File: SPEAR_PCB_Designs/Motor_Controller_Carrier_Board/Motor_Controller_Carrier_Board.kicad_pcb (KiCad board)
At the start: 2 copper layers, 7 parts, among them J1 Conn_01x02_Pin, J2 Conn_01x02_Pin, J3 Conn_01x02_Pin

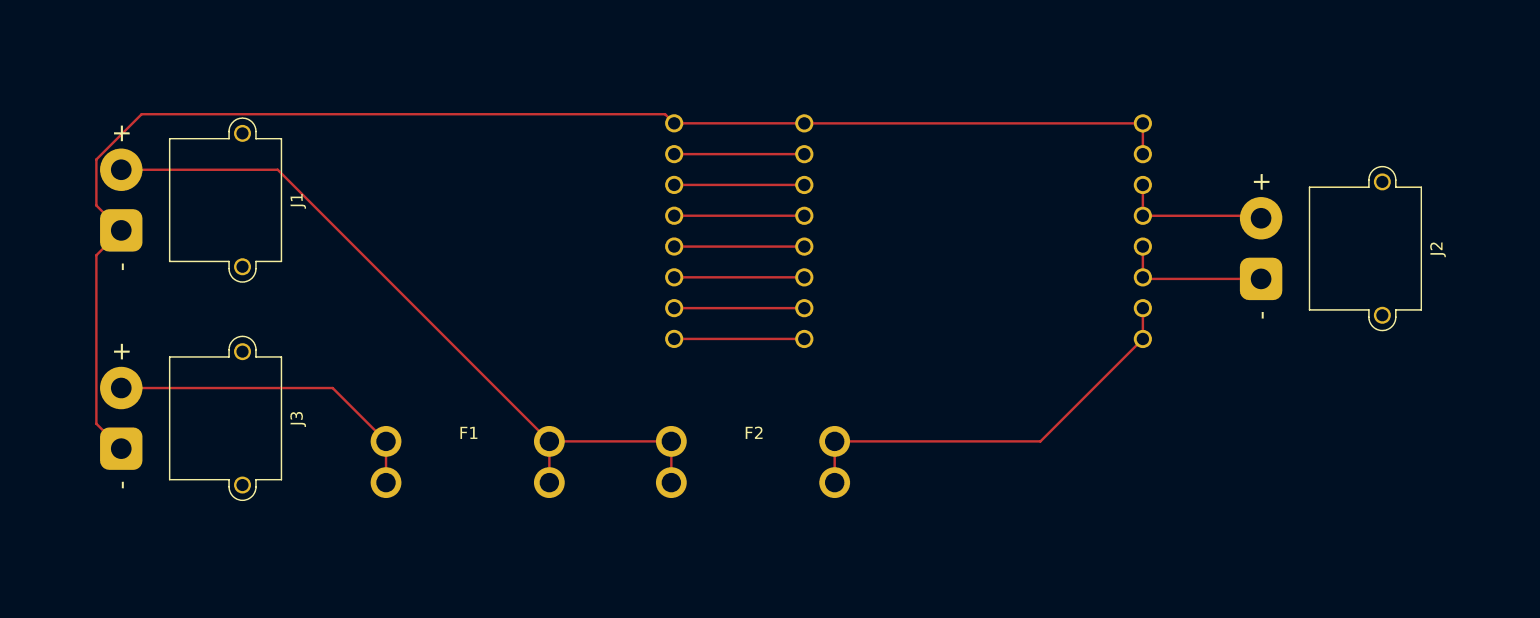
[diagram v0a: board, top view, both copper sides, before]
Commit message: added Carrier Board PCB
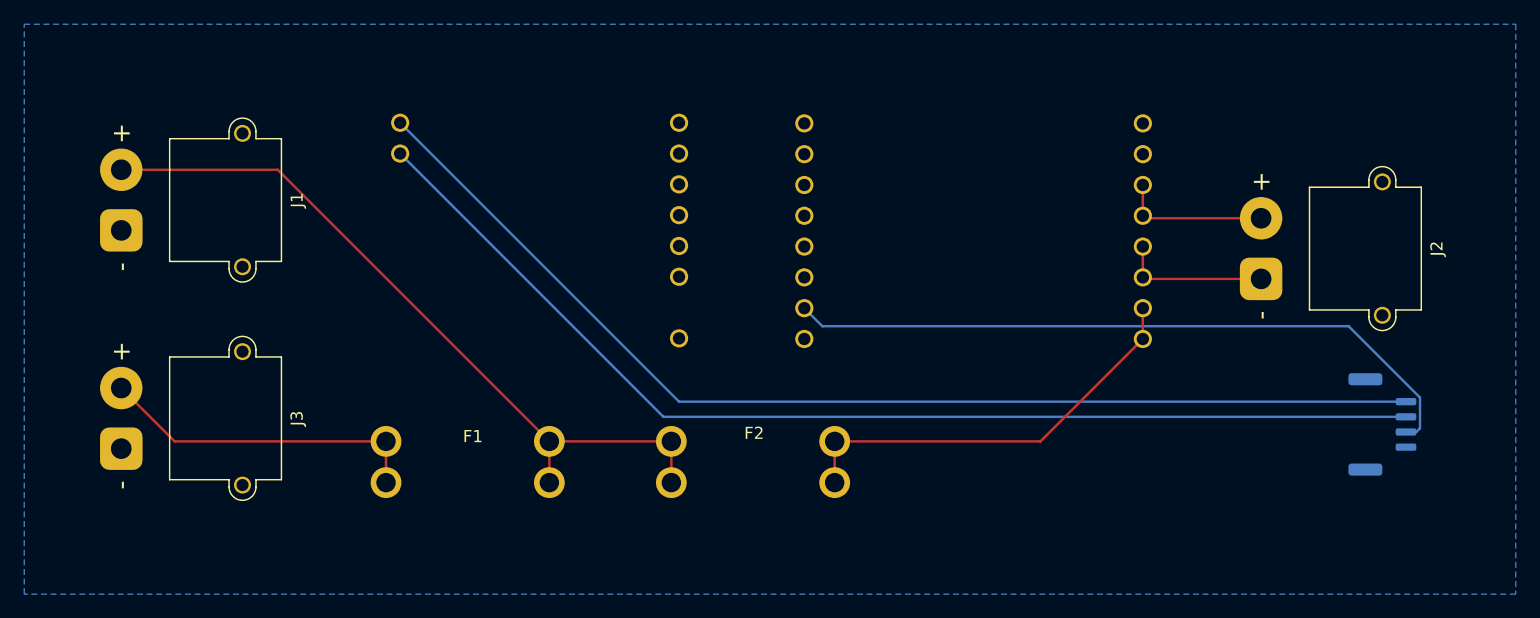
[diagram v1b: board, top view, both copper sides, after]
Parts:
- added J4: Conn_01x04_Pin, Motor_Controller_Carrier_Board:JST_GH_BM04B-GHS-TBT_1x04-1MP_P1.25mm_Vertical, B.Cu at (176.0, 103.0)
- moved MiCB1 0.40 mm to (90.0, 76.9)
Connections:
- net Net-(J1-Pin_1) renamed GND
- MDB1 pad 7: Net-(MDB1-3V3) -> Net-(J4-Pin_3)
- MiCB1 pad 7: Net-(MDB1-3V3) -> Net-(MDB1-VM)
- MiCB1 pad 8: Net-(MDB1-VM) -> Net-(J4-Pin_1)
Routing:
- net GND: track 117.1 -> 0.00 mm
- net Net-(J4-Pin_1): track 0.00 -> 92.5 mm
- net Net-(J4-Pin_2): track 0.00 -> 91.9 mm
- net Net-(J4-Pin_3): track 0.00 -> 57.6 mm
- net Net-(MDB1-DIR): track 10.7 -> 0.00 mm
- net Net-(MDB1-3V3): track 10.7 -> 0.00 mm
- net Net-(MDB1-VM): track 10.7 -> 0.00 mm
- net Net-(MDB1-SLP): track 10.7 -> 0.00 mm
- net Net-(MDB1-PWM): track 10.7 -> 0.00 mm
- net Net-(MDB1-FLT): track 10.7 -> 0.00 mm
- net Net-(MDB1-CS): track 10.7 -> 0.00 mm
- net Net-(J2-Pin_2): track 12.4 -> 13.7 mm
- added copper zone on B.Cu, net GND

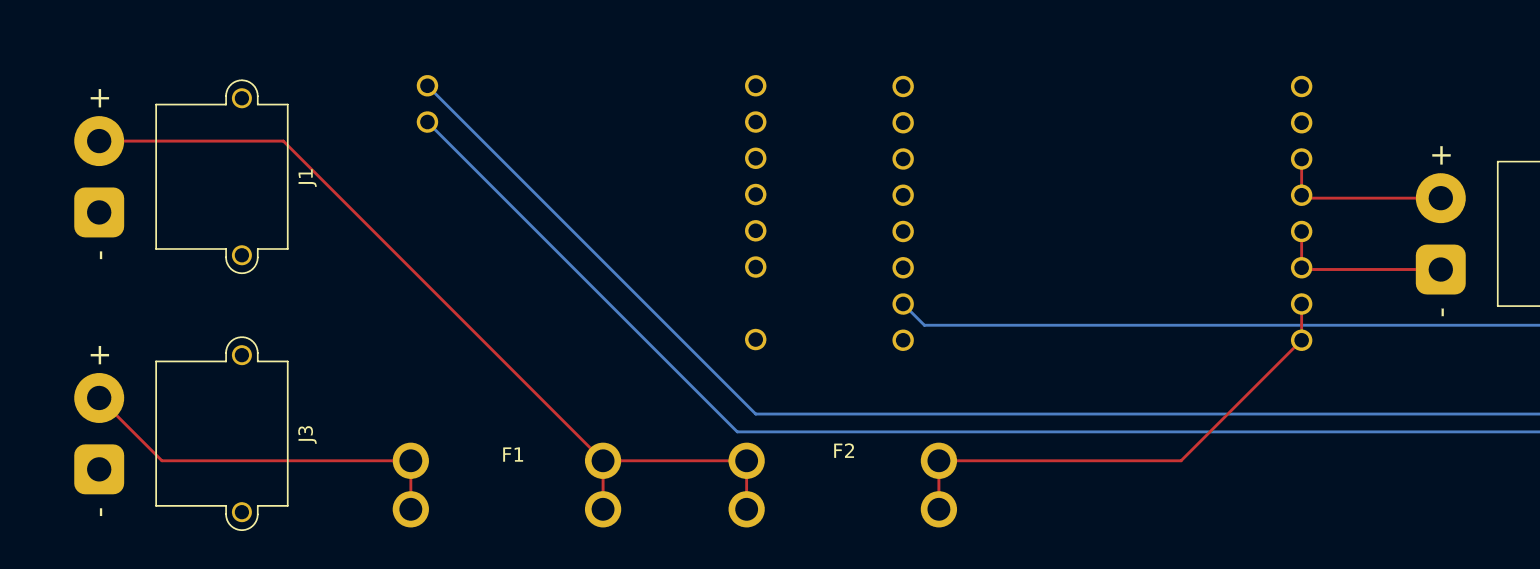
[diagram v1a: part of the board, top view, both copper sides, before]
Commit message: moved board footprints and created new motor driver board footprints
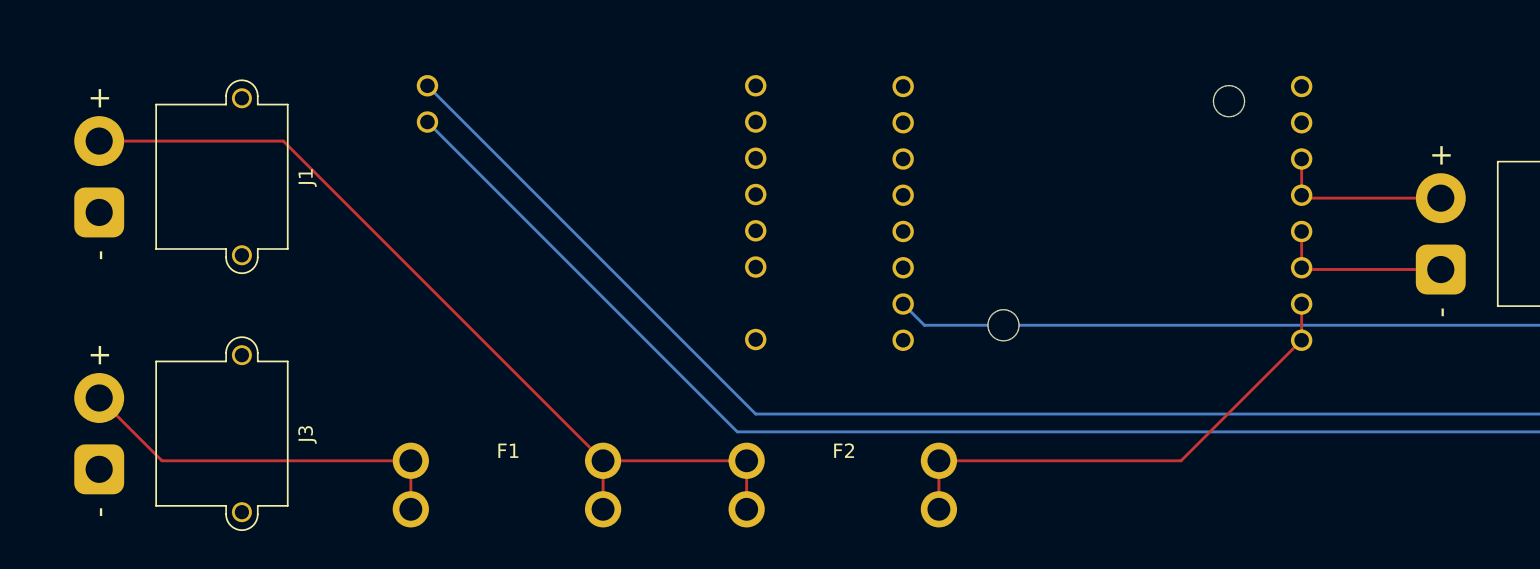
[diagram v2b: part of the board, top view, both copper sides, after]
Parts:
- J1, J2, J3: footprint XT30:AMASS_XT30PW-M -> Connector_AMASS:AMASS_XT30PW-M_1x02_P2.50mm_Horizontal
- MDB1: footprint Motor_Controller_Carrier_Board:Motor_Driver_Board -> SPEAR_Boards:Motor_Driver_Board_2992
- MiCB1: footprint Motor_Controller_Carrier_Board:Micro_Controller_Board -> SPEAR_Boards:Micro_Controller_Board

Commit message: Finished schematic and general PCB layout for carrier board 2992
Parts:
- removed MiCB1: Micro_Controller_Board, SPEAR_Boards:Micro_Controller_Board
- added C1: 10u, SPEAR_AP63203BuckConverter:CAP_FG20_TDK_C1, F.Cu at (106.8, 81.0)
- added C2: 22u, SPEAR_AP63203BuckConverter:CAP_FG22_TDK_C2_C4, F.Cu at (108.0, 51.5)
- added C3: 100n, Capacitor_THT:C_Disc_D5.0mm_W2.5mm_P5.00mm, F.Cu at (106.2, 73.0)
- added C4: 22u, SPEAR_AP63203BuckConverter:CAP_FG22_TDK_C2_C4, F.Cu at (102.5, 51.5)
- added C5: C, Motor_Controller_Carrier_Board:CAP_UBY_18X20_NCH, F.Cu at (162.0, 100.5)
- added L1: 3.9u, SPEAR_AP63203BuckConverter:L_Wurth_WE-LHMI-1040_L1, F.Cu at (104.0, 65.0)
- added MCB1: Micro_Controller_Board, SPEAR_Boards:Micro_Controller_Board, F.Cu at (167.7, 50.0)
- added U1: AP63203WU, Package_TO_SOT_SMD:TSOT-23-6, F.Cu at (102.0, 78.1)
- F1, F2: value Fuse -> 3557-10; footprint Motor_Controller_Carrier_Board:Fuse -> Motor_Controller_Carrier_Board:FUSE_3557-10
- J4: value Conn_01x04_Pin -> JST_S4B-XH-A-1; footprint Motor_Controller_Carrier_Board:JST_GH_BM04B-GHS-TBT_1x04-1MP_P1.25mm_Vertical -> Connector_JST:JST_XH_S4B-XH-A-1_1x04_P2.50mm_Horizontal; moved to F.Cu
- MDB1: value Motor_Driver_Board -> Motor_Driver_Board_2992
- moved J3 104.2 mm to (176.0, 111.0)
- moved J2 67.0 mm to (99.0, 89.0), turned to 90 degrees
- moved MDB1 64.0 mm to (190.1, 65.6), turned to -90 degrees
- moved J4 42.5 mm to (174.0, 60.5), turned to 90 degrees
- moved J1 32.5 mm to (98.7, 105.5), turned to 90 degrees
- moved F1 26.4 mm to (117.0, 105.0), turned to 90 degrees
- moved F2 6.60 mm to (108.0, 105.0), turned to 90 degrees
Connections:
- J2 pad 1: Net-(J2-Pin_1) -> GND
- J3 pad 1: GND -> Net-(J3-Pin_1)
- J4 pad 1: Net-(J4-Pin_1) -> /ENC_B
- J4 pad 2: Net-(J4-Pin_2) -> /ENC_A
- J4 pad 3: Net-(J4-Pin_3) -> GND
- J4 pad 4: GND -> +3.3V
- MDB1 pad 11: Net-(J2-Pin_2) -> Net-(J3-Pin_2)
- MDB1 pad 12: Net-(J2-Pin_2) -> Net-(J3-Pin_2)
- MDB1 pad 13: Net-(J2-Pin_1) -> Net-(J3-Pin_1)
- MDB1 pad 14: Net-(J2-Pin_1) -> Net-(J3-Pin_1)
- MDB1 pad 15: Net-(F2-Pad2) -> +BATT
- MDB1 pad 16: Net-(F2-Pad2) -> +BATT
- MDB1 pad 2: Net-(MDB1-DIR) -> /DIR
- MDB1 pad 3: Net-(MDB1-PWM) -> /PWM
- MDB1 pad 4: Net-(MDB1-SLP) -> /SLP
- MDB1 pad 5: Net-(MDB1-FLT) -> /FLT
- MDB1 pad 6: Net-(MDB1-CS) -> /CS
- MDB1 pad 7: Net-(J4-Pin_3) -> unconnected-(MDB1-3V3-Pad7)
- MDB1 pad 8: Net-(MDB1-VM) -> unconnected-(MDB1-VM-Pad8)
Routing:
- net +3.3V: track 0.00 -> 102.0 mm
- net Net-(J4-Pin_1): track 92.5 -> 0.00 mm
- net Net-(J4-Pin_2): track 91.9 -> 0.00 mm
- net +BATT: track 0.00 -> 85.2 mm
- net /ENC_B: track 0.00 -> 61.7 mm
- net Net-(J4-Pin_3): track 57.6 -> 0.00 mm
- net /CS: track 0.00 -> 48.5 mm
- net Net-(J1-Pin_2): track 61.4 -> 20.5 mm
- net /FLT: track 0.00 -> 35.6 mm
- net Net-(F2-Pad2): track 34.9 -> 0.00 mm
- net /SLP: track 0.00 -> 34.7 mm
- net /PWM: track 0.00 -> 34.1 mm
- net /DIR: track 0.00 -> 33.8 mm
- net /ENC_A: track 0.00 -> 28.4 mm
- net Net-(J3-Pin_1): track 0.00 -> 21.3 mm
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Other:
- board outline added: 192 x 103 mm

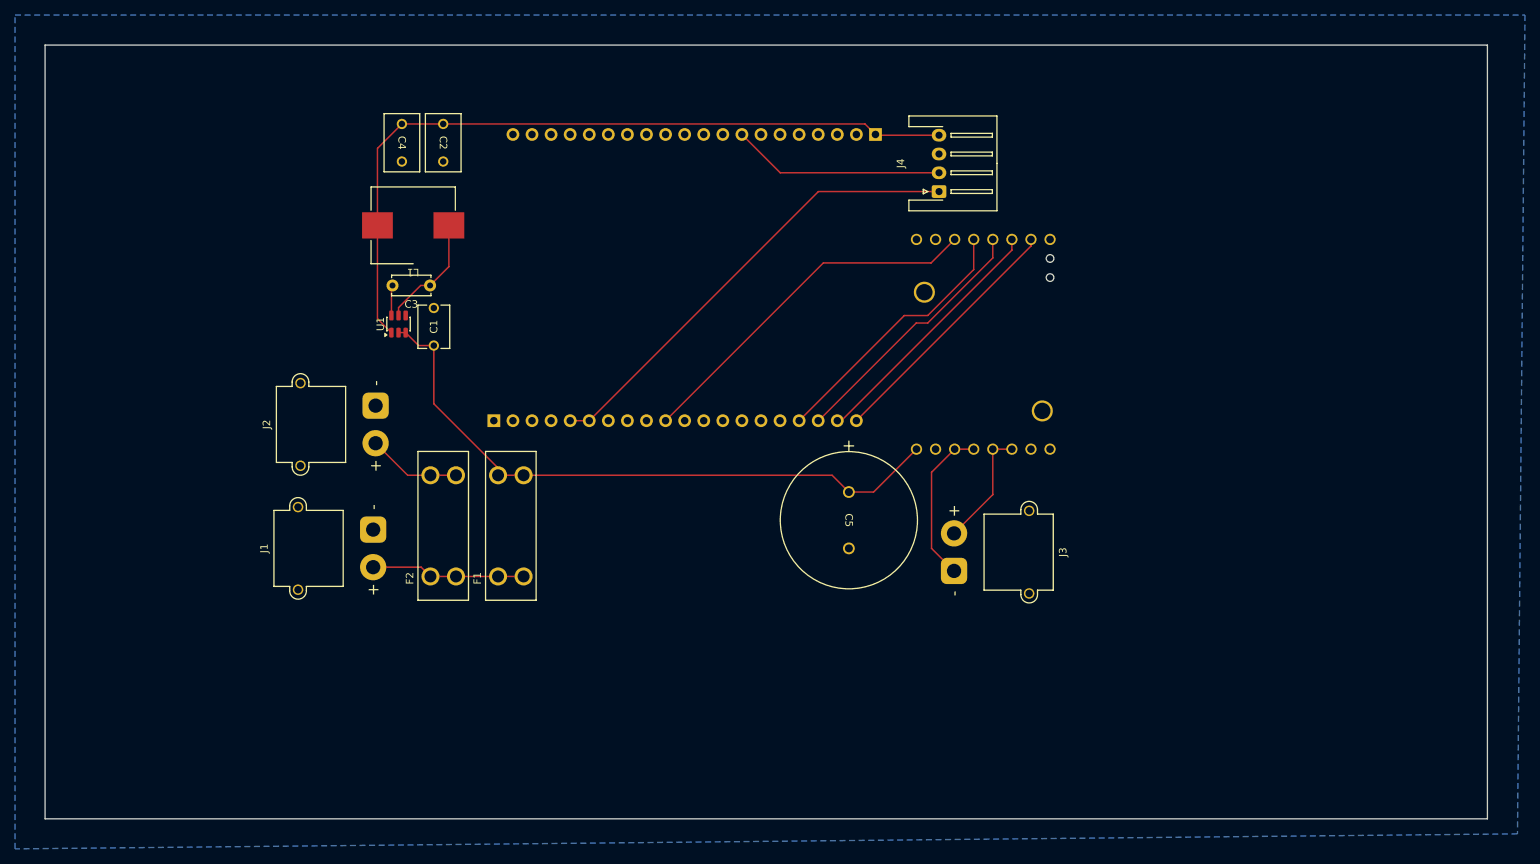
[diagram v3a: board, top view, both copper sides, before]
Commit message: Added silkscreen and courtyards to board footprints and 3D models to the carrier board
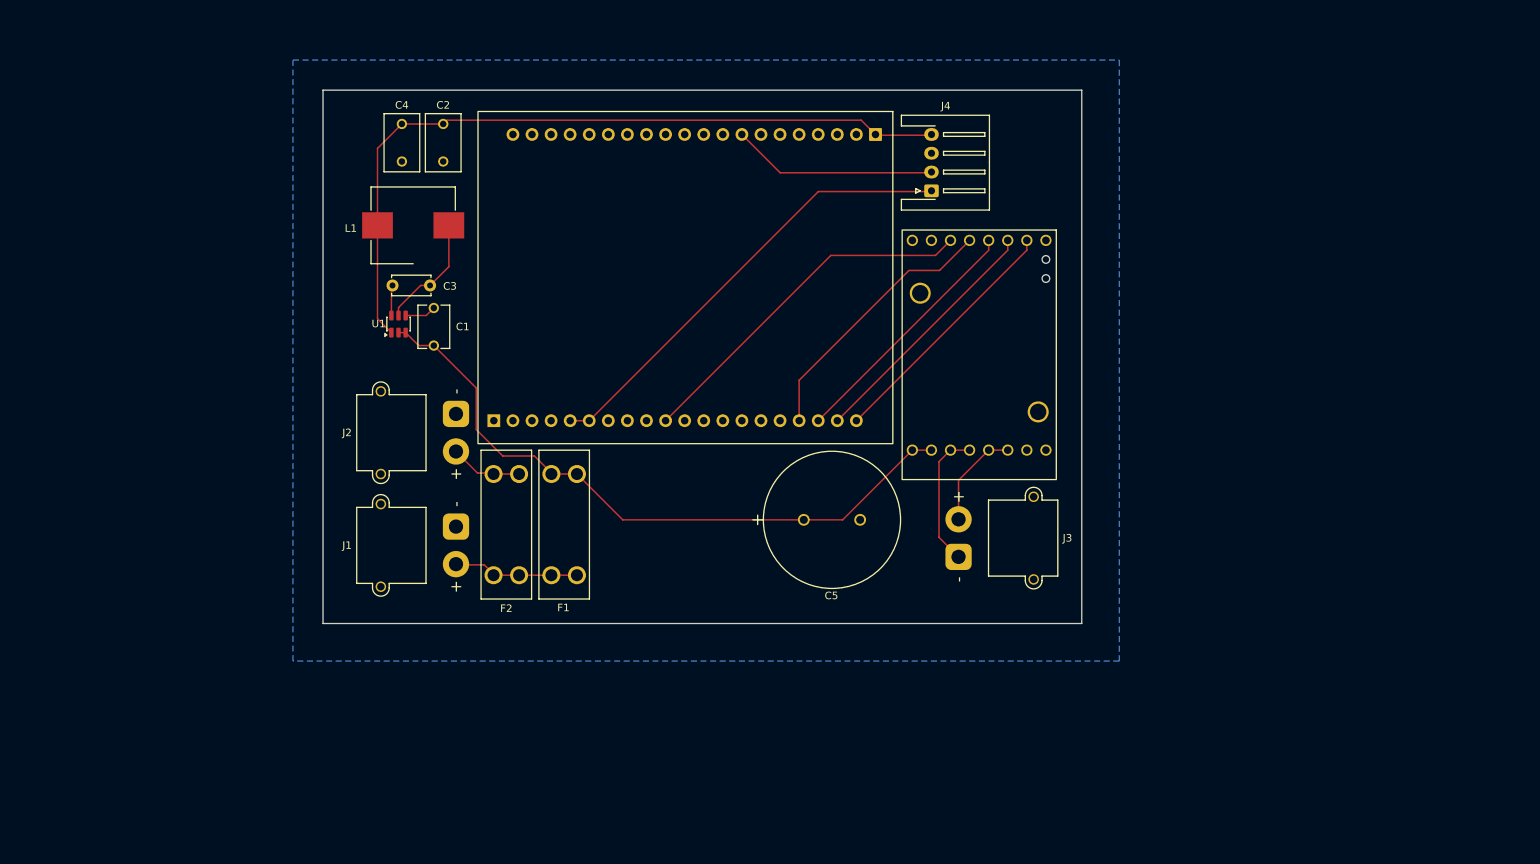
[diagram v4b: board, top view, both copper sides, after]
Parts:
- F2: value 3557-10 -> 3557-15; footprint Motor_Controller_Carrier_Board:FUSE_3557-10 -> Motor_Controller_Carrier_Board:FUSE_3557-15
- moved J1 11.0 mm to (109.7, 105.1)
- moved J2 10.8 mm to (109.7, 90.1)
- moved F2 8.40 mm to (116.4, 104.8)
- moved F1 7.10 mm to (124.1, 104.8)
- moved C5 7.05 mm to (156.0, 104.2), turned to 0 degrees
- moved J3 1.96 mm to (176.6, 109.1)
- moved J4 1.00 mm to (173.0, 60.4)
- moved MDB1 0.57 mm to (189.5, 65.7)
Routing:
- net GND: track 0.00 -> 4.16 mm
- net Net-(J1-Pin_2): track 20.5 -> 16.8 mm
- net +BATT: track 85.2 -> 88.4 mm
- net Net-(J2-Pin_2): track 12.5 -> 9.64 mm
- net Net-(J3-Pin_1): track 21.3 -> 18.5 mm
- net Net-(J3-Pin_2): track 15.9 -> 13.4 mm
- net /SLP: track 34.7 -> 33.4 mm
- net /ENC_A: track 28.4 -> 27.4 mm
- net /ENC_B: track 61.7 -> 60.8 mm
- net /PWM: track 34.1 -> 33.4 mm
- net /CS: track 48.5 -> 47.9 mm
- net +3.3V: track 102.0 -> 101.5 mm
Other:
- board size 192 x 103 mm -> 101 x 71 mm
